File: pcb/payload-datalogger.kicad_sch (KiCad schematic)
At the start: 30 parts, among them J1 2.54mm 01x02 header, J2 DE15 Socket, SW2 PTS815, U1 XIAO-ESP32-C3-DIP, U2 NCP177AMX330TCG, U3 W25X40CLSN

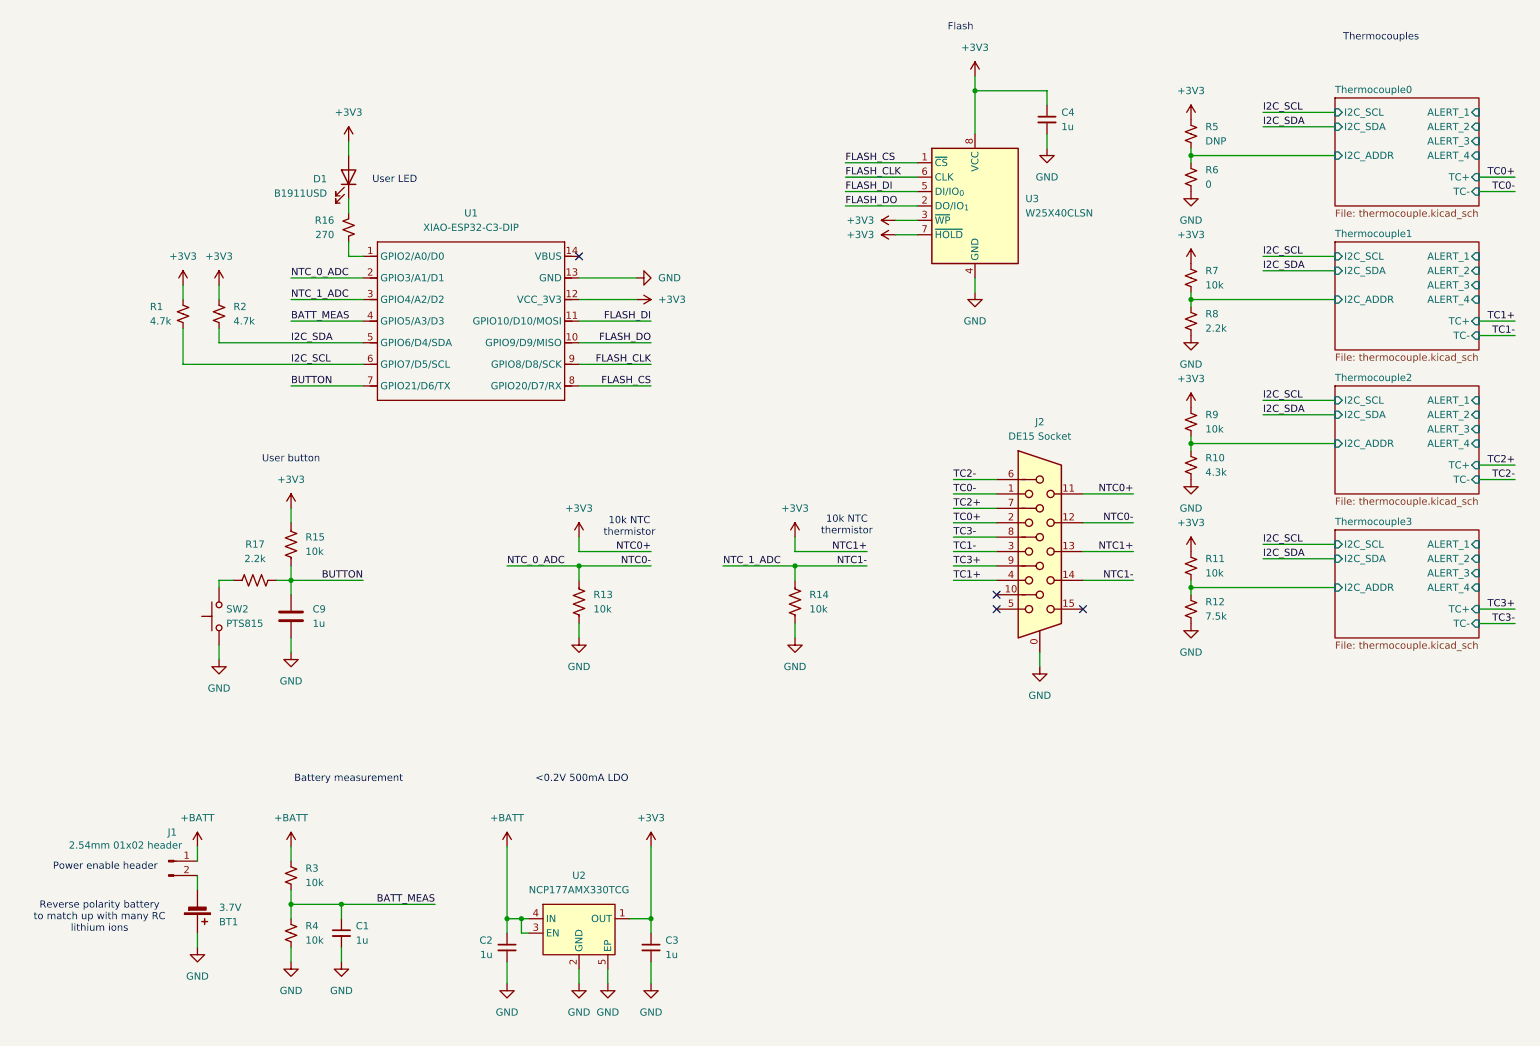
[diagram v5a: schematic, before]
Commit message: Switch to ESP32 C3 WROOM module
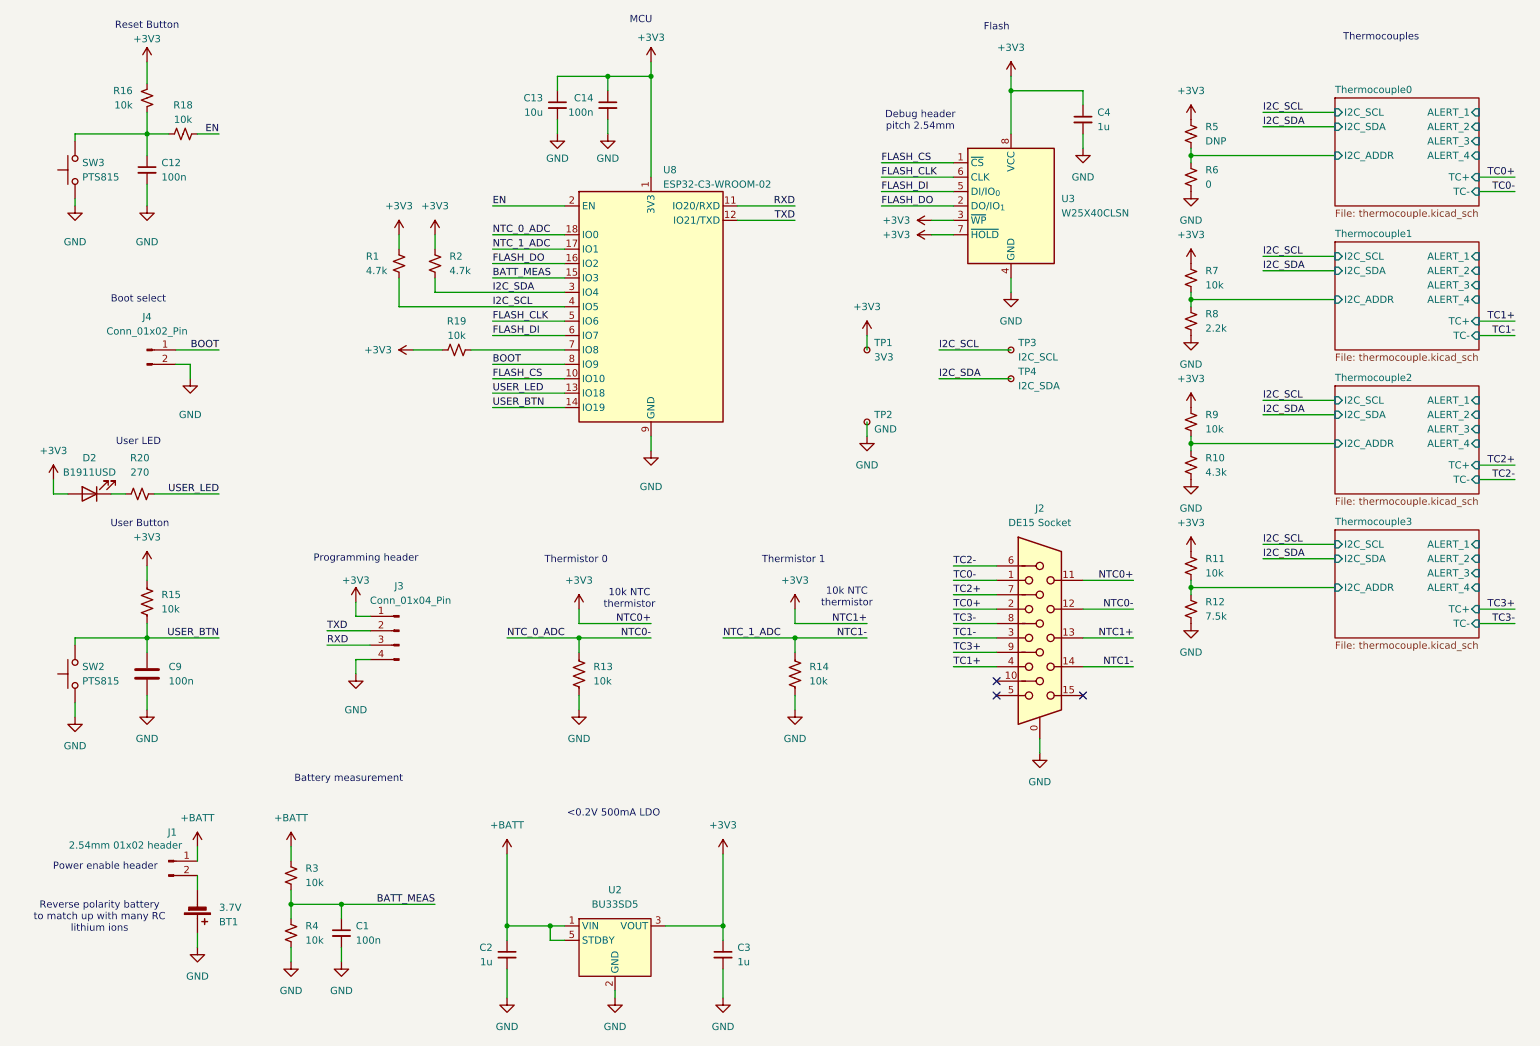
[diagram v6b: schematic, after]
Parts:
- removed D1: B1911USD, LED_SMD:LED_0603_1608Metric, symbol Device:LED
- removed R17: 2.2k, Resistor_SMD:R_0603_1608Metric, symbol Device:R_US
- removed U1: XIAO-ESP32-C3-DIP, Seeed Studio XIAO Series Library:XIAO-ESP32C3-DIP, symbol Seeed_Studio_XIAO_Series:XIAO-ESP32-C3-DIP
- removed U2: NCP177AMX330TCG, Package_DFN_QFN:OnSemi_XDFN4-1EP_1.0x1.0mm_EP0.52x0.52mm, symbol NCP177AMX330TCG:NCP177AMX330TCG
- added C12, C14: 100n, Capacitor_SMD:C_0603_1608Metric, symbol Device:C_Small
- added C13: 10u, Capacitor_SMD:C_0603_1608Metric, symbol Device:C_Small
- added D2: B1911USD, LED_SMD:LED_0603_1608Metric, symbol Device:LED
- added J3: Conn_01x04_Pin, Connector_PinHeader_2.54mm:PinHeader_1x04_P2.54mm_Vertical, symbol Connector:Conn_01x04_Pin
- added J4: Conn_01x02_Pin, Connector_PinHeader_2.54mm:PinHeader_1x02_P2.54mm_Vertical, symbol Connector:Conn_01x02_Pin
- added R18, R19: 10k, Resistor_SMD:R_0603_1608Metric, symbol Device:R_Small_US
- added R20: 270, Resistor_SMD:R_0603_1608Metric, symbol Device:R_Small_US
- added SW3: PTS815, PTS815_SJM_250_SMTR_LFS:SW_Push_PTS815_SJM_250_SMTR_LFS, symbol Switch:SW_Push
- added TP1: 3V3, TestPoint:TestPoint_Pad_D1.0mm, symbol Connector:TestPoint_Small
- added TP2: GND, TestPoint:TestPoint_Pad_D1.0mm, symbol Connector:TestPoint_Small
- added TP3: I2C_SCL, TestPoint:TestPoint_Pad_D1.0mm, symbol Connector:TestPoint_Small
- added TP4: I2C_SDA, TestPoint:TestPoint_Pad_D1.0mm, symbol Connector:TestPoint_Small
- added U2: BU33SD5, BUxxSD5:SSOP5_ROM, symbol BUxxSD5:BU33SD5
- added U8: ESP32-C3-WROOM-02, RF_Module:ESP32-C3-WROOM-02, symbol RF_Module:ESP32-C3-WROOM-02
- C1, C9: value 1u -> 100n
- R16: value 270 -> 10k
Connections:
- net BUTTON is gone; now on net USER_BTN: C9.1, R15.2
- net +3V3: now also R16.2, C13.1, C14.1, D2.2 (A), J3.1 (Pin_1), R19.1, TP1.1, U2.3 (VOUT), U8.1 (3V3)
- net +BATT: now also U2.1 (VIN), U2.5 (STDBY)
- net BATT_MEAS: now also U8.15 (IO3)
- net FLASH_CLK: now also U8.5 (IO6)
- net FLASH_CS: now also U8.10 (IO10)
- net FLASH_DI: now also U8.6 (IO7)
- net FLASH_DO: now also U8.16 (IO2)
- net GND: now also C12.2, C13.2, C14.2, J3.4 (Pin_4), J4.2 (Pin_2), SW3.1, TP2.1, U2.2 (GND), U8.19 (GND), U8.9 (GND)
- net I2C_SCL: now also TP3.1, U8.4 (IO5)
- net I2C_SDA: now also TP4.1, U8.3 (IO4)
- net NTC0-: now also U8.18 (IO0)
- net NTC1-: now also U8.17 (IO1)
- net at R16.1: now also C12.1, R18.1, SW3.2
- net USER_BTN: now reaches SW2.2
- net USER_BTN: now also U8.14 (IO19)
- new net: R19.2, U8.7 (IO8)
- new net: D2.1 (K), R20.1
- new net BOOT: J4.1 (Pin_1), U8.8 (IO9)
- new net EN: R18.2, U8.2 (EN)
- new net RXD: J3.3 (Pin_3), U8.11 (IO20/RXD)
- new net TXD: J3.2 (Pin_2), U8.12 (IO21/TXD)
- new net USER_LED: R20.2, U8.13 (IO18)
- no-connect marks 4 -> 3
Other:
- note added: "Boot select"
- note added: "Debug header pitch 2.54mm"
- note added: "MCU"
- note added: "Programming header"
- note added: "Reset Button"
- note added: "Thermistor 0"
- note added: "Thermistor 1"
- note added: "User Button"
- note removed: "User button"
- moved on the sheet: C2, C3, C4, C9, J2, R1, R13, R14, R15, R2, SW2, U3
